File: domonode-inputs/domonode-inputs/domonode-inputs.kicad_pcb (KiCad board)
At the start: 2 copper layers, 95 x 80 mm, 66 parts, among them P1 CONN_01X02, P10 CONN_01X02, P11 CONN_01X02, P12 CONN_02X03, P13 CONN_02X05, P14 CONN_01X06, P2 CONN_01X02, P3 CONN_01X02, P4 CONN_01X02, P5 CONN_01X02, P6 CONN_01X02, P7 CONN_01X02, P8 CONN_01X02, P9 CONN_01X02, U1 TLP620, U10 TLP620, U11 PCA9555, U12 24LC02, U13 TLP620, U2 TLP620, U3 TLP620, U4 TLP620, U5 TLP620, U6 TLP620, U7 TLP620, U8 TLP620, U9 TLP620

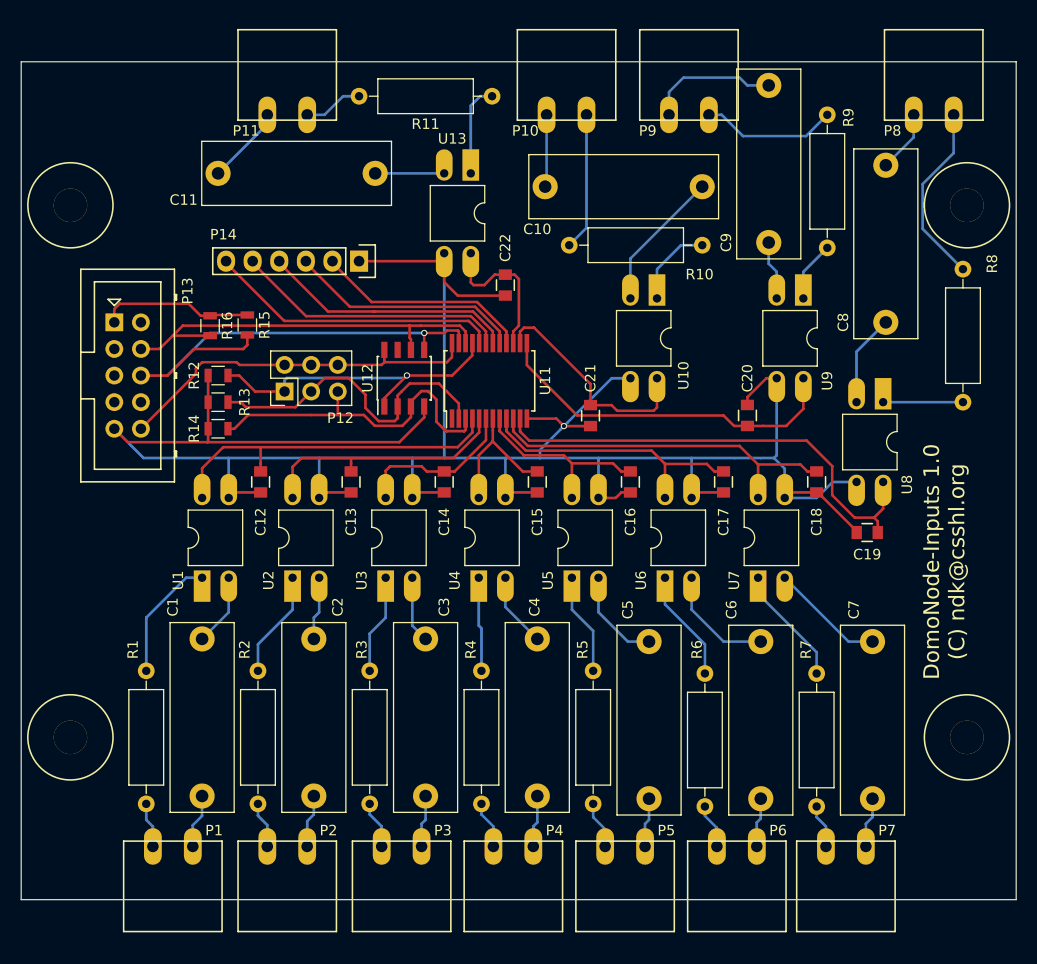
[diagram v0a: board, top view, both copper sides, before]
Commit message: Reorganized DomoNode-Inputs files and added gerbers
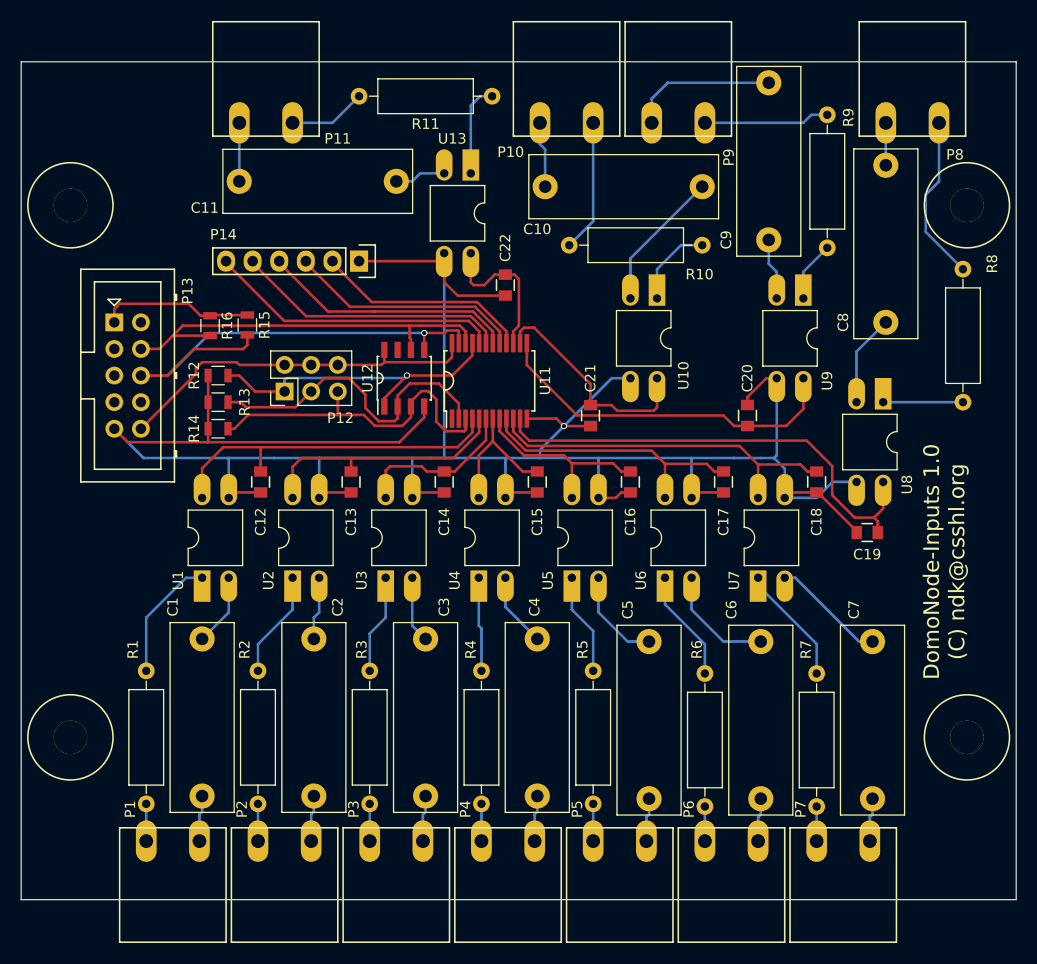
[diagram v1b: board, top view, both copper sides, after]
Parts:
- P1, P10, P11, P2, P3, P4, P5, P6, P7, P8, P9: footprint AAA mie lib verificate:KF2EDGK-3.81-2 -> AAA mie lib verificate:KF2EDGK-5.08-2
- U11: footprint Housings_SSOP:SSOP-24_5.3x8.2mm_Pitch0.65mm -> AAA mie lib verificate:SSOP-24_5.3x8.2mm_Pitch0.65mm
- U12: footprint Housings_SOIC:SOIC-8_3.9x4.9mm_Pitch1.27mm -> AAA mie lib verificate:SOIC-8_3.9x4.9mm_Pitch1.27mm
- moved P3 4.98 mm to (173.5, 100.8), turned to 0 degrees
- moved P4 4.98 mm to (184.2, 100.8), turned to 0 degrees
- moved P6 4.98 mm to (205.5, 100.8), turned to 0 degrees
- moved P5 4.98 mm to (194.8, 100.8), turned to 0 degrees
- moved P2 4.73 mm to (162.8, 100.8), turned to 0 degrees
- moved P7 4.73 mm to (216.2, 100.8), turned to 0 degrees
- moved P10 4.51 mm to (194.8, 32.3), turned to 180 degrees
- moved P1 4.47 mm to (152.1, 100.8), turned to 0 degrees
- moved P9 3.51 mm to (205.5, 32.3), turned to 180 degrees
- moved P11 2.53 mm to (166.1, 32.3), turned to 180 degrees
- moved P8 2.53 mm to (227.8, 32.3), turned to 180 degrees
- moved C11 2.16 mm to (176.0, 37.8)
- moved C9 0.25 mm to (211.6, 43.4)
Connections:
- P1 pad 1: Net-(C1-Pad2) -> Net-(P1-Pad1)
- P1 pad 2: Net-(P1-Pad2) -> Net-(C1-Pad2)
- P10 pad 1: Net-(C10-Pad2) -> Net-(P10-Pad1)
- P10 pad 2: Net-(P10-Pad2) -> Net-(C10-Pad2)
- P11 pad 1: Net-(C11-Pad2) -> Net-(P11-Pad1)
- P11 pad 2: Net-(P11-Pad2) -> Net-(C11-Pad2)
- P2 pad 1: Net-(C2-Pad2) -> Net-(P2-Pad1)
- P2 pad 2: Net-(P2-Pad2) -> Net-(C2-Pad2)
- P3 pad 1: Net-(C3-Pad2) -> Net-(P3-Pad1)
- P3 pad 2: Net-(P3-Pad2) -> Net-(C3-Pad2)
- P4 pad 1: Net-(C4-Pad2) -> Net-(P4-Pad1)
- P4 pad 2: Net-(P4-Pad2) -> Net-(C4-Pad2)
- P5 pad 1: Net-(C5-Pad2) -> Net-(P5-Pad1)
- P5 pad 2: Net-(P5-Pad2) -> Net-(C5-Pad2)
- P6 pad 1: Net-(C6-Pad2) -> Net-(P6-Pad1)
- P6 pad 2: Net-(P6-Pad2) -> Net-(C6-Pad2)
- P7 pad 1: Net-(C7-Pad2) -> Net-(P7-Pad1)
- P7 pad 2: Net-(P7-Pad2) -> Net-(C7-Pad2)
- P8 pad 1: Net-(C8-Pad2) -> Net-(P8-Pad1)
- P8 pad 2: Net-(P8-Pad2) -> Net-(C8-Pad2)
- P9 pad 1: Net-(C9-Pad2) -> Net-(P9-Pad1)
- P9 pad 2: Net-(P9-Pad2) -> Net-(C9-Pad2)
- R1 pad 2: Net-(P1-Pad2) -> Net-(P1-Pad1)
- R10 pad 2: Net-(P10-Pad2) -> Net-(P10-Pad1)
- R11 pad 2: Net-(P11-Pad2) -> Net-(P11-Pad1)
- R2 pad 2: Net-(P2-Pad2) -> Net-(P2-Pad1)
- R3 pad 2: Net-(P3-Pad2) -> Net-(P3-Pad1)
- R4 pad 2: Net-(P4-Pad2) -> Net-(P4-Pad1)
- R5 pad 2: Net-(P5-Pad2) -> Net-(P5-Pad1)
- R6 pad 2: Net-(P6-Pad2) -> Net-(P6-Pad1)
- R7 pad 2: Net-(P7-Pad2) -> Net-(P7-Pad1)
- R8 pad 2: Net-(P8-Pad2) -> Net-(P8-Pad1)
- R9 pad 2: Net-(P9-Pad2) -> Net-(P9-Pad1)
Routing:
- net Net-(P8-Pad2): track 17.8 -> 0.00 mm
- net Net-(P8-Pad1): track 0.00 -> 16.0 mm
- net Net-(P10-Pad2): track 13.1 -> 0.00 mm
- net Net-(P9-Pad2): track 13.0 -> 0.00 mm
- net Net-(P10-Pad1): track 0.00 -> 12.6 mm
- net Net-(P9-Pad1): track 0.00 -> 12.0 mm
- net Net-(P11-Pad1): track 0.00 -> 7.40 mm
- net Net-(P11-Pad2): track 5.69 -> 0.00 mm
- net Net-(P5-Pad2): track 4.54 -> 0.00 mm
- net Net-(P4-Pad2): track 4.54 -> 0.00 mm
- net Net-(P3-Pad2): track 4.54 -> 0.00 mm
- net Net-(P2-Pad2): track 4.43 -> 0.00 mm
- net Net-(P1-Pad2): track 4.33 -> 0.00 mm
- net Net-(P6-Pad2): track 4.28 -> 0.00 mm
- net Net-(P7-Pad2): track 4.18 -> 0.00 mm
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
